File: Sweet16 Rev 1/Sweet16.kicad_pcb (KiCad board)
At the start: 2 copper layers, 140 x 60 mm, 67 parts, among them J1 Conn_01x09_Male, J10 SW_half_inverter, J11 R_clock, J12 OUT_clock, J13 SW_dual8_hex, J14 OUT_OUT, J15 R_sync_pitch_1, J16 SW_sync_1, J17 R_sync_pitch_2, J18 SW_sync_2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

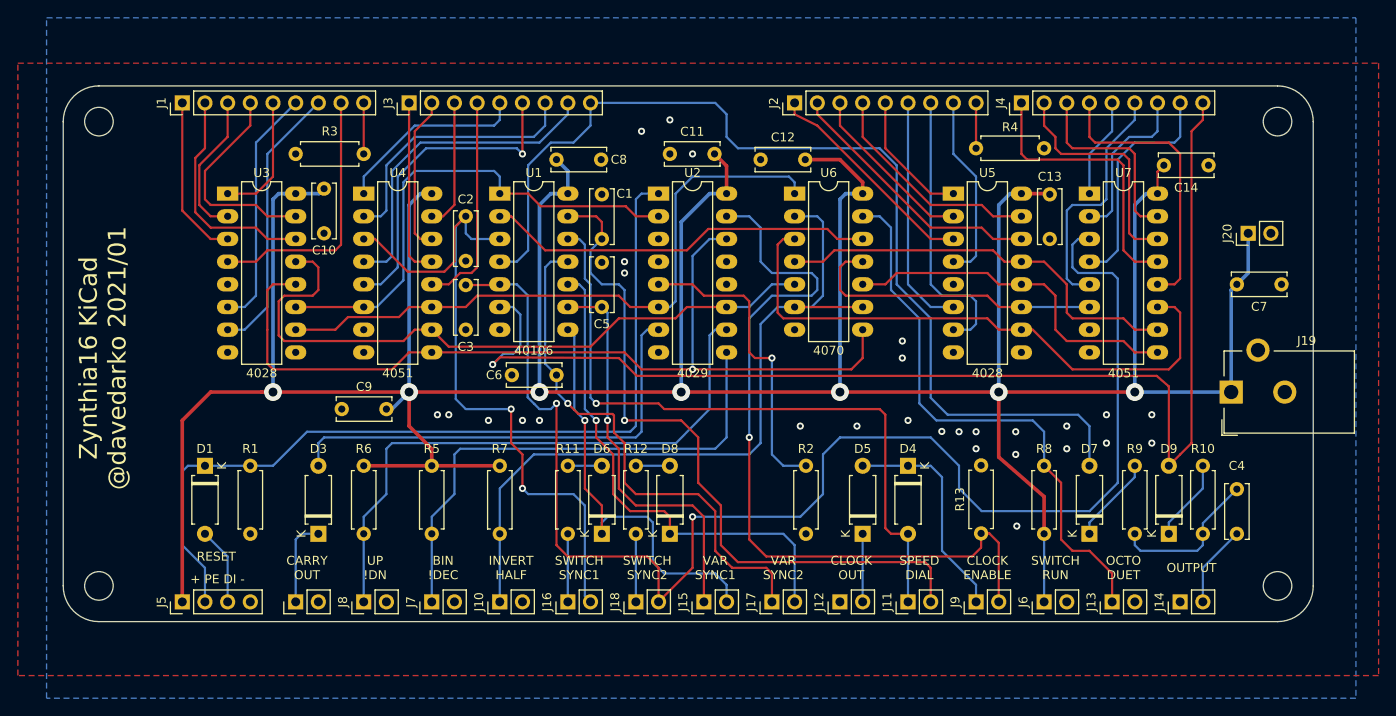
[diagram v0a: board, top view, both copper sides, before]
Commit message: moved bits added labels
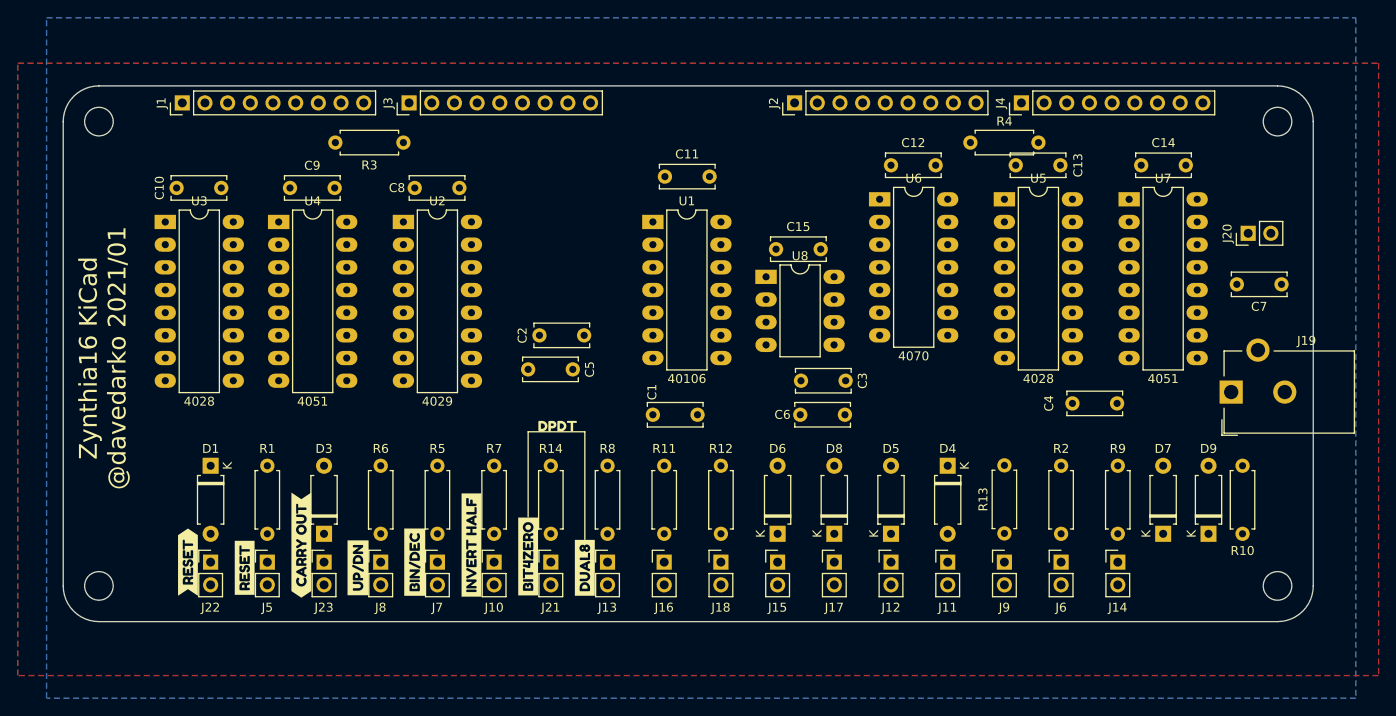
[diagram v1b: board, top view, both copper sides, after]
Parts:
- removed OUT_CARRY_OUT1: Conn_01x02_Male, Connector_PinHeader_2.54mm:PinHeader_1x02_P2.54mm_Vertical
- added C15: C, Capacitor_THT:C_Disc_D6.0mm_W2.5mm_P5.00mm, F.Cu at (79.8, 18.3)
- added J21: SW_dual8_hex_2, Connector_PinHeader_2.54mm:PinHeader_1x02_P2.54mm_Vertical, F.Cu at (54.6, 53.3)
- added J22: OUT_OUT, Connector_PinHeader_2.54mm:PinHeader_1x02_P2.54mm_Vertical, F.Cu at (16.5, 53.3)
- added J23: OUT_CARRY_OUT, Connector_PinHeader_2.54mm:PinHeader_1x02_P2.54mm_Vertical, F.Cu at (29.2, 53.3)
- added R14: 4700R, Resistor_THT:R_Axial_DIN0207_L6.3mm_D2.5mm_P7.62mm_Horizontal, F.Cu at (54.6, 50.2)
- added U8: TL072, Package_DIP:DIP-8_W7.62mm_LongPads, F.Cu at (78.7, 21.4)
- added kibuzzard-610C1637: G***, label, F.Cu at (26.7, 51.4)
- added kibuzzard-610C1856: G***, label, F.Cu at (33.0, 54.0)
- added kibuzzard-610C1A63: G***, label, F.Cu at (39.4, 53.3)
- added kibuzzard-610C1AC8: G***, label, F.Cu at (45.7, 51.4)
- added kibuzzard-610C1D73: G***, label, F.Cu at (20.3, 54.0)
- added kibuzzard-610C1E26: G***, label, F.Cu at (14.0, 53.3)
- added kibuzzard-610C2350: G***, label, F.Cu at (58.4, 54.0)
- added kibuzzard-610C23E8: G***, label, F.Cu at (52.1, 52.7)
- added kibuzzard-610C2455: G***, label, F.Cu at (55.4, 38.1)
- J5: value Conn_01x04_Male -> OUT_OUT; footprint Connector_PinHeader_2.54mm:PinHeader_1x04_P2.54mm_Vertical -> Connector_PinHeader_2.54mm:PinHeader_1x02_P2.54mm_Vertical
- moved J13 56.7 mm to (61.0, 53.3), turned to 0 degrees
- moved R8 49.5 mm to (61.0, 50.2), turned to 90 degrees
- moved C3 39.0 mm to (82.6, 33.0), turned to 0 degrees
- moved C6 32.6 mm to (82.5, 36.8)
- moved U2 28.8 mm to (38.1, 15.2)
- moved R2 28.6 mm to (111.8, 42.5)
- moved C9 25.4 mm to (25.4, 11.4)
- moved C1 22.4 mm to (71.0, 36.8), turned to 180 degrees
- moved C8 21.1 mm to (39.4, 11.4), turned to 0 degrees
- moved C4 19.8 mm to (118.0, 35.6), turned to 180 degrees
- moved D6 19.7 mm to (80.0, 50.2)
- moved D8 18.4 mm to (86.4, 50.2)
- moved U1 17.4 mm to (66.0, 15.2)
- moved C10 17.3 mm to (12.7, 11.4), turned to 0 degrees
- moved C2 15.7 mm to (53.3, 27.9), turned to 0 degrees
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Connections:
- J12 pad 1: GND -> Net-(D5-Pad1)
- J12 pad 2: Net-(D5-Pad1) -> GND
- J14 pad 1: GND -> Net-(C4-Pad1)
- J14 pad 2: Net-(C4-Pad1) -> GND
- J5 pad 1: VCC -> Net-(D1-Pad1)
- J5 pad 2: Net-(D1-Pad1) -> VCC
- J6 pad 2: GND -> Net-(J6-Pad2)
- R2 pad 1: Net-(R2-Pad1) -> GND
- R2 pad 2: GND -> Net-(J6-Pad2)
- U2 pad 2: QD1 -> Net-(J21-Pad1)
- U2 pad 5: Net-(R2-Pad1) -> Net-(J6-Pad2)
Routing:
- net VCC: track 410.5 -> 0.00 mm, vias 7 -> 0
- net Net-(C3-Pad1): track 159.5 -> 0.00 mm, vias 2 -> 0
- net Net-(D9-Pad2): track 138.6 -> 0.00 mm, vias 1 -> 0
- net Net-(D7-Pad2): track 114.5 -> 0.00 mm
- net QC1: track 101.2 -> 0.00 mm, vias 1 -> 0
- net Net-(D1-Pad1): track 96.8 -> 0.00 mm
- net Net-(J9-Pad2): track 88.0 -> 0.00 mm, vias 1 -> 0
- net Net-(J10-Pad1): track 85.0 -> 0.00 mm
- net Net-(C1-Pad1): track 80.0 -> 0.00 mm, vias 1 -> 0
- net Net-(C2-Pad1): track 79.6 -> 0.00 mm, vias 2 -> 0
- net Net-(D4-Pad2): track 76.5 -> 0.00 mm, vias 1 -> 0
- net QB1: track 76.4 -> 0.00 mm
- net QA1: track 72.6 -> 0.00 mm
- net Net-(J8-Pad1): track 66.7 -> 0.00 mm
- net QA2: track 65.9 -> 0.00 mm
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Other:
- board text removed: "+ PE DI -"
- board text removed: "BIN !DEC"
- board text removed: "CARRY OUT"
- board text removed: "CLOCK ENABLE"
- board text removed: "CLOCK OUT"
- board text removed: "INVERT HALF"
- board text removed: "OCTO DUET"
- board text removed: "OUTPUT"
- board text removed: "RESET"
- board text removed: "SPEED DIAL"
- board text removed: "SWITCH RUN"
- board text removed: "SWITCH SYNC1"
- board text removed: "SWITCH SYNC2"
- board text removed: "UP !DN"
- board text removed: "VAR SYNC1"
- board text removed: "VAR SYNC2"

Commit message: labels
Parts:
- added kibuzzard-610C51A7: G***, label, F.Cu at (64.8, 54.0)
- added kibuzzard-610C51E0: G***, label, F.Cu at (71.1, 54.0)
- added kibuzzard-610C523D: G***, label, F.Cu at (83.8, 53.3)
- added kibuzzard-610C5269: G***, label, F.Cu at (77.5, 53.3)
- added kibuzzard-610C52EC: G***, label, F.Cu at (15.9, 4.45)
- added kibuzzard-610C530B: G***, label, F.Cu at (85.1, 4.45)
- added kibuzzard-610C5339: G***, label, F.Cu at (111.8, 4.45)
- added kibuzzard-610C5373: G***, label, F.Cu at (43.2, 4.45)
- added kibuzzard-610C5418: G***, label, F.Cu at (90.2, 51.4)
- added kibuzzard-610C545E: G***, label, F.Cu at (102.9, 52.1)
- added kibuzzard-610C5562: G***, label, F.Cu at (96.5, 53.3)
- added kibuzzard-610C55EA: G***, label, F.Cu at (109.2, 54.0)
- added kibuzzard-610C561B: G***, label, F.Cu at (115.6, 52.7)
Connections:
- J15 pad 1: Net-(C5-Pad2) -> Net-(D6-Pad1)
- J15 pad 2: Net-(D6-Pad1) -> Net-(C5-Pad2)
- J17 pad 1: Net-(C6-Pad2) -> Net-(D8-Pad1)
- J17 pad 2: Net-(D8-Pad1) -> Net-(C6-Pad2)
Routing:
- net QB1: track 0.00 -> 41.1 mm
- net QC1: track 0.00 -> 38.6 mm
- net QA1: track 0.00 -> 20.1 mm
- net Net-(D1-Pad1): track 0.00 -> 15.7 mm
- net QD1: track 0.00 -> 5.33 mm
- net Net-(J16-Pad1): track 0.00 -> 3.81 mm
- net Net-(J8-Pad1): track 0.00 -> 3.18 mm
- net Net-(J7-Pad1): track 0.00 -> 3.18 mm
- net Net-(J21-Pad1): track 0.00 -> 3.18 mm
- net Net-(J18-Pad1): track 0.00 -> 3.18 mm
- net Net-(J13-Pad1): track 0.00 -> 3.18 mm
- net Net-(J10-Pad1): track 0.00 -> 3.18 mm
- net Net-(D8-Pad1): track 0.00 -> 3.18 mm
- net Net-(D6-Pad1): track 0.00 -> 3.18 mm
- net Net-(D5-Pad1): track 0.00 -> 3.18 mm
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
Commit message: 48 wires to go
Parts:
- removed D7, D9: D, Diode_THT:D_A-405_P7.62mm_Horizontal
- removed J19: Barrel_Jack, Connector_BarrelJack:BarrelJack_CUI_PJ-102AH_Horizontal
- removed R10, R9: R, Resistor_THT:R_Axial_DIN0207_L6.3mm_D2.5mm_P7.62mm_Horizontal
- added R15: 100k, Resistor_THT:R_Axial_DIN0207_L6.3mm_D2.5mm_P7.62mm_Horizontal, F.Cu at (123.8, 27.3)
- added R16: 100k, Resistor_THT:R_Axial_DIN0207_L6.3mm_D2.5mm_P7.62mm_Horizontal, F.Cu at (131.4, 31.8)
- added kibuzzard-6111A8BD: G***, label, F.Cu at (121.9, 52.7)
- U8: value TL072 -> LM358
- moved J6 76.2 mm to (35.6, 53.3)
- moved R2 76.2 mm to (35.6, 42.5)
- moved kibuzzard-610C55EA 76.2 mm to (33.0, 54.0)
- moved C15 45.8 mm to (125.1, 11.4)
- moved U8 45.5 mm to (123.8, 15.2)
- moved J20 37.7 mm to (124.5, 53.3), turned to 0 degrees
- moved C7 29.2 mm to (124.5, 48.8), turned to 90 degrees
- moved C3 27.8 mm to (55.9, 25.4), turned to 180 degrees
- moved C5 25.6 mm to (77.4, 27.9), turned to 180 degrees
- moved C13 23.9 mm to (82.9, 11.4)
- moved U5 23.9 mm to (81.7, 15.2)
- moved C1 19.1 mm to (72.5, 17.8), turned to 0 degrees
- moved kibuzzard-610C1AC8 19.1 mm to (64.8, 51.4)
- moved J10 19.1 mm to (67.3, 53.3)
- moved R7 19.1 mm to (67.3, 50.2)
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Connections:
- J3 pad 9: Net-(D7-Pad2) -> Net-(J3-Pad9)
- J4 pad 9: Net-(D9-Pad2) -> Net-(J4-Pad9)
- U1 pad 4: Net-(D7-Pad2) -> Net-(J3-Pad9)
- U1 pad 6: Net-(D9-Pad2) -> Net-(J4-Pad9)
- U8 pad 1: Net-(U8-Pad1) -> Net-(R16-Pad1)
- U8 pad 2: Net-(U8-Pad2) -> Net-(R16-Pad1)
- U8 pad 3: Net-(U8-Pad3) -> Net-(J4-Pad9)
- U8 pad 5: Net-(U8-Pad5) -> Net-(J3-Pad9)
- U8 pad 6: Net-(U8-Pad6) -> Net-(R15-Pad2)
- U8 pad 7: Net-(U8-Pad7) -> Net-(R15-Pad2)
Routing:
- net VCC: track 0.00 -> 170.6 mm
- net Net-(J1-Pad8): track 0.00 -> 54.6 mm
- net Net-(J2-Pad8): track 0.00 -> 53.0 mm
- net Net-(J1-Pad7): track 0.00 -> 40.4 mm
- net Net-(J2-Pad7): track 0.00 -> 38.5 mm
- net Net-(J6-Pad2): track 0.00 -> 37.7 mm
- net Net-(J1-Pad6): track 0.00 -> 36.8 mm
- net Net-(J3-Pad6): track 0.00 -> 35.5 mm
- net Net-(J3-Pad8): track 0.00 -> 35.5 mm
- net Net-(J2-Pad6): track 0.00 -> 35.3 mm
- net Net-(J4-Pad6): track 0.00 -> 35.0 mm
- net Net-(J1-Pad2): track 0.00 -> 32.8 mm
- net Net-(D1-Pad1): track 15.7 -> 48.0 mm
- net Net-(J4-Pad8): track 0.00 -> 31.7 mm
- net Net-(J2-Pad2): track 0.00 -> 31.6 mm
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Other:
- board text added: "Zynthia16 KiCad @davedarko 2021/08"
- board text removed: "Zynthia16 KiCad @davedarko 2021/01"

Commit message: routed, but untested
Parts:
- moved J9 82.6 mm to (29.2, 53.3)
- moved R13 82.6 mm to (29.2, 50.1)
- moved kibuzzard-610C5562 82.6 mm to (20.3, 53.3)
- moved D4 82.5 mm to (22.9, 42.5)
- moved D5 82.5 mm to (16.5, 50.2)
- moved J11 82.5 mm to (22.9, 53.3)
- moved J12 82.5 mm to (16.5, 53.3)
- moved kibuzzard-610C5418 82.5 mm to (14.0, 51.4)
- moved kibuzzard-610C545E 82.5 mm to (26.7, 52.1)
- moved D8 19.1 mm to (111.8, 50.2)
- moved J17 19.1 mm to (111.8, 53.3)
- moved kibuzzard-610C5269 19.1 mm to (102.9, 53.3)
- moved J13 19.1 mm to (80.0, 53.3)
- moved J7 19.1 mm to (61.0, 53.3)
- moved J8 19.1 mm to (67.3, 53.3)
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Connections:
- U1 pad 3: Net-(C2-Pad1) -> Net-(C3-Pad1)
- U1 pad 4: Net-(J3-Pad9) -> Net-(J4-Pad9)
- U1 pad 5: Net-(C3-Pad1) -> Net-(C2-Pad1)
- U1 pad 6: Net-(J4-Pad9) -> Net-(J3-Pad9)
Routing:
- net VCC: track 170.6 -> 388.5 mm
- net Net-(C3-Pad1): track 0.00 -> 156.6 mm
- net Net-(J3-Pad9): track 0.00 -> 130.4 mm, vias 0 -> 2
- net QC1: track 23.5 -> 151.0 mm
- net Net-(J4-Pad9): track 0.00 -> 119.4 mm, vias 0 -> 2
- net Net-(J21-Pad1): track 3.18 -> 101.3 mm
- net Net-(C2-Pad1): track 0.00 -> 91.7 mm
- net Net-(C1-Pad1): track 0.00 -> 86.5 mm
- net Net-(J13-Pad1): track 3.18 -> 88.1 mm
- net QD1: track 23.1 -> 105.4 mm, vias 0 -> 1
- net QB1: track 17.3 -> 99.4 mm, vias 0 -> 1
- net Net-(C6-Pad2): track 0.00 -> 78.6 mm
- net QA1: track 32.7 -> 105.6 mm
- net Net-(D4-Pad2): track 3.18 -> 75.0 mm
- net Net-(D8-Pad1): track 3.18 -> 72.6 mm
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
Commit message: probably done
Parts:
- added kibuzzard-6112EA2B: G***, label, F.Cu at (14.6, 36.2)
- added kibuzzard-6112EA3D: G***, label, F.Cu at (85.7, 36.2)
- added kibuzzard-6112EA56: G***, label, F.Cu at (29.8, 36.2)
- added kibuzzard-6112EA78: G***, label, F.Cu at (43.2, 36.2)
- added kibuzzard-6112EA8E: G***, label, F.Cu at (113.7, 36.2)
- added kibuzzard-6112EAB9: G***, label, F.Cu at (64.1, 36.2)
- added kibuzzard-6112EAC9: G***, label, F.Cu at (99.7, 36.2)
- added kibuzzard-6112EADF: G***, label, F.Cu at (127.6, 26.0)
- added kibuzzard-6112EDB2: G***, label, F.Cu at (8.26, 26.0)
- added kibuzzard-6112EDD8: G***, label, F.Cu at (23.5, 26.0)
- added kibuzzard-6112EDF7: G***, label, F.Cu at (36.8, 26.7)
- added kibuzzard-6112EE23: G***, label, F.Cu at (107.3, 26.7)
- added kibuzzard-6112EE9D: G***, label, F.Cu at (57.8, 25.4)
- added kibuzzard-6112EEB7: G***, label, F.Cu at (79.4, 26.0)
- added kibuzzard-6112EED9: G***, label, F.Cu at (134.0, 19.1)
- added kibuzzard-6112EEFB: G***, label, F.Cu at (93.3, 26.0)
- added kibuzzard-6112F4A3: G***, label, F.Cu at (74.9, 15.1)
- added kibuzzard-6112F4D1: G***, label, F.Cu at (53.3, 22.9)
- added kibuzzard-6112F4F2: G***, label, F.Cu at (53.3, 17.8)
- added kibuzzard-6112F51D: G***, label, F.Cu at (74.9, 25.4)
- added kibuzzard-6112F530: G***, label, F.Cu at (74.9, 20.3)
- moved R16 3.81 mm to (131.4, 35.6)
- moved R15 3.18 mm to (123.8, 30.5)
- moved kibuzzard-610C2455 0.63 mm to (74.4, 37.5)
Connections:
- net Net-(J21-Pad1) renamed QD0
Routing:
- net Net-(R16-Pad1): track 22.3 -> 26.1 mm
- net Net-(C4-Pad2): track 19.6 -> 15.8 mm
- net Net-(R15-Pad2): track 13.9 -> 17.0 mm
- net Net-(C2-Pad1): track 91.7 -> 93.9 mm
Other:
- board text added: "A1"
- board text added: "A2"
- board text added: "B1"
- board text added: "B2"
- board text added: "C1"
- board text added: "C2"
- board text added: "D0"
- board text added: "D1"
- board text added: "D2"
- board text added: "LM358"

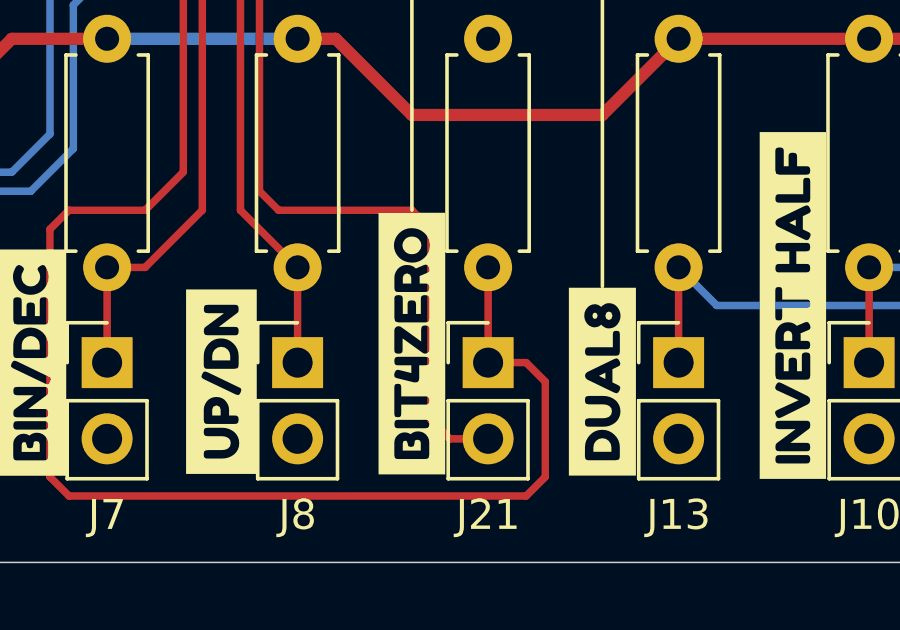
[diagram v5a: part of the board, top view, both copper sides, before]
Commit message: fixed pulldown AND kept all buzzard labels
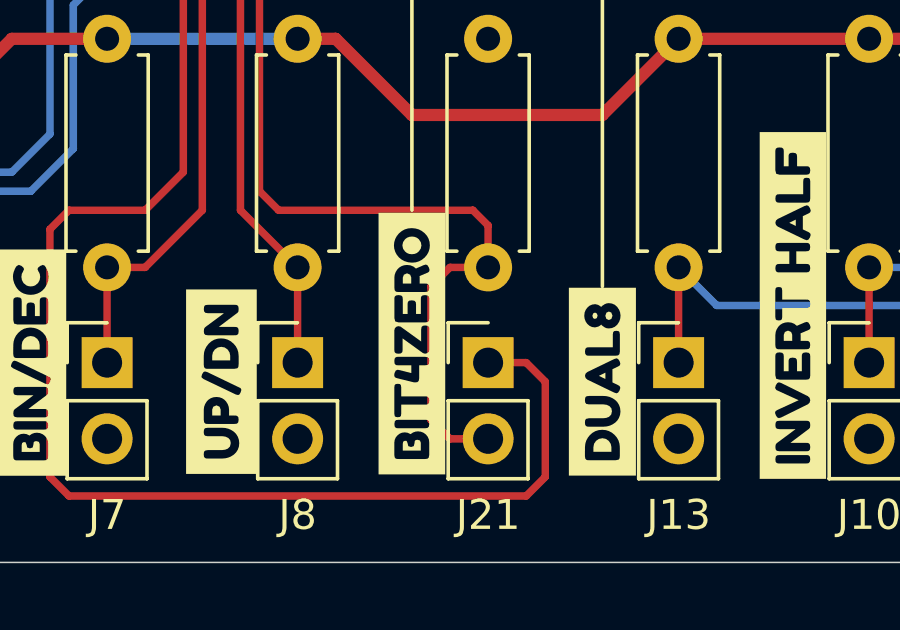
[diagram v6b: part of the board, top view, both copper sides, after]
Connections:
- R14 pad 1: QD0 -> QD1
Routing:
- net QD1: track 105.4 -> 108.9 mm
- net QD0: track 101.3 -> 98.1 mm
